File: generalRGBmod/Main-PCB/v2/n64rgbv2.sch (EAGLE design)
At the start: 76 parts, among them J3 2510-, U1 5M570ZT100C5, U2 ADV7125/ADV7123, U4 TLV70018-DDC

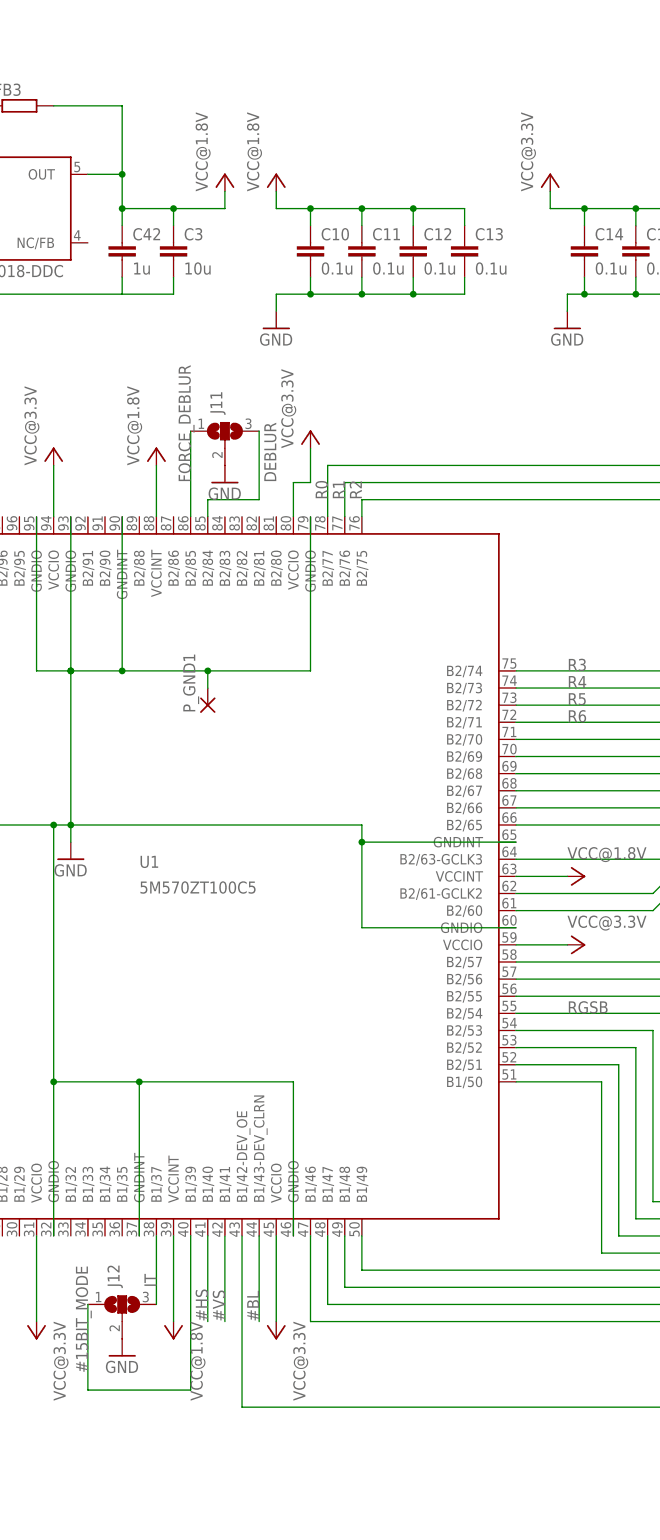
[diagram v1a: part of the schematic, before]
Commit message: N64RGBv1/v2 misc updates  (thanks to iFixRetro for giving feedback here!!!): - bugfix BOM and silkscreen (N64RGBv2) - silkscreen update to distinguish between MaxII and MaxV setup avoiding assembly mistakes - move power regulator to BOT copper side (N64RGBv1) - additional jumper J1 to select between 240LE and 570LE CPLD (for proper usage of the 5M240ZT)
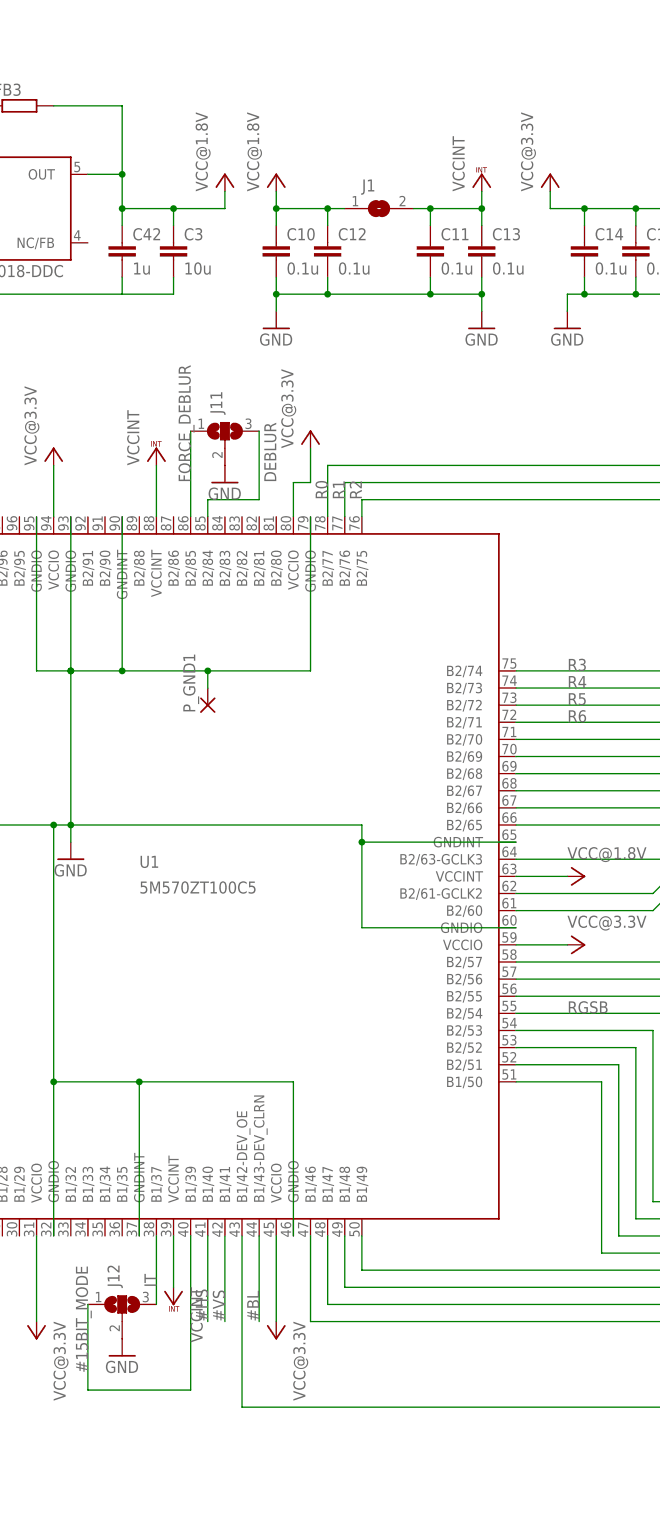
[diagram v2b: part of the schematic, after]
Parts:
- added J1: (no value), jumper:SJ
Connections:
- new net VCCINT: C11.1, C13.1, J1.2, U1.VCCINT@2, U1.VCCINT@3
- net VCC@1.8V: now also J1.1; no longer C11.1, C13.1, U1.VCCINT@2, U1.VCCINT@3
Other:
- moved on the sheet: C10, C11, C12, C13
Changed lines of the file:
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@@
 <?xml version="1.0" encoding="utf-8"?>
 <!DOCTYPE eagle SYSTEM "eagle.dtd">
-<eagle version="8.4.3">
+<eagle version="8.5.0">
 <drawing>
 <settings>
@@
 <part name="C17" library="rcl" deviceset="C-EU" device="C0603" value="0.1u"/>
 <part name="U1" library="altera" deviceset="5M570ZT100C5" device=""/>
-<part name="P+15" library="supply1" library_urn="urn:adsk.eagle:library:371" deviceset="VCC" device="" value="VCC@1.8V"/>
-<part name="P+16" library="supply1" library_urn="urn:adsk.eagle:library:371" deviceset="VCC" device="" value="VCC@1.8V"/>
 <part name="C18" library="rcl" deviceset="C-EU" device="C0603" value="0.1u"/>
 <part name="C19" library="rcl" deviceset="C-EU" device="C0603" value="0.1u"/>
@@
 <part name="J12" library="jumper" deviceset="SJ2W" device=""/>
 <part name="FB3" library="rcl" deviceset="R-EU_" device="R0603"/>
+<part name="VCC1" library="supply1" library_urn="urn:adsk.eagle:library:371" deviceset="VCCINT" device=""/>
+<part name="GND2" library="supply1" library_urn="urn:adsk.eagle:library:371" deviceset="GND" device=""/>
+<part name="VCC2" library="supply1" library_urn="urn:adsk.eagle:library:371" deviceset="VCCINT" device=""/>
+<part name="VCC3" library="supply1" library_urn="urn:adsk.eagle:library:371" deviceset="VCCINT" device=""/>
+<part name="J1" library="jumper" deviceset="SJ" device=""/>
 </parts>
 <sheets>
@@
 <instance part="CTRL" gate="1" x="15.24" y="101.6"/>
 <instance part="RST#" gate="1" x="7.62" y="99.06"/>
-<instance part="C11" gate="G$1" x="175.26" y="215.9"/>
+<instance part="C11" gate="G$1" x="185.42" y="215.9"/>
 <instance part="FB1" gate="G$1" x="78.74" y="220.98"/>
 <instance part="P+3" gate="VCC" x="93.98" y="226.06"/>
@@
 <instance part="P_VCC0" gate="1" x="55.88" y="220.98"/>
 <instance part="P_GND0" gate="1" x="55.88" y="208.28"/>
-<instance part="C12" gate="G$1" x="182.88" y="215.9"/>
-<instance part="C13" gate="G$1" x="190.5" y="215.9"/>
+<instance part="C12" gate="G$1" x="170.18" y="215.9"/>
+<instance part="C13" gate="G$1" x="193.04" y="215.9"/>
 <instance part="C14" gate="G$1" x="208.28" y="215.9"/>
 <instance part="C15" gate="G$1" x="215.9" y="215.9"/>
@@
 <instance part="C17" gate="G$1" x="231.14" y="215.9"/>
 <instance part="U1" gate="G$1" x="144.78" y="121.92"/>
-<instance part="P+15" gate="VCC" x="144.78" y="185.42"/>
-<instance part="P+16" gate="VCC" x="147.32" y="53.34" rot="R180"/>
 <instance part="C18" gate="G$1" x="238.76" y="215.9"/>
 <instance part="C19" gate="G$1" x="246.38" y="215.9"/>
-<instance part="C10" gate="G$1" x="167.64" y="215.9"/>
+<instance part="C10" gate="G$1" x="162.56" y="215.9"/>
 <instance part="C1" gate="G$1" x="66.04" y="215.9"/>
 <instance part="C2" gate="G$1" x="93.98" y="215.9"/>
@@
 <instance part="J12" gate="G$1" x="139.7" y="58.42" rot="R90"/>
 <instance part="FB3" gate="G$1" x="124.46" y="236.22"/>
+<instance part="VCC1" gate="G$1" x="193.04" y="226.06"/>
+<instance part="GND2" gate="1" x="193.04" y="203.2"/>
+<instance part="VCC2" gate="G$1" x="144.78" y="185.42"/>
+<instance part="VCC3" gate="G$1" x="147.32" y="58.42" rot="R180"/>
+<instance part="J1" gate="1" x="177.8" y="220.98"/>
 </instances>
 <busses>
@@
 </segment>
 <segment>
-<pinref part="C11" gate="G$1" pin="2"/>
-<wire x1="175.26" y1="210.82" x2="175.26" y2="208.28" width="0.1524" layer="91"/>
-<wire x1="175.26" y1="208.28" x2="167.64" y2="208.28" width="0.1524" layer="91"/>
-<wire x1="167.64" y1="208.28" x2="162.56" y2="208.28" width="0.1524" layer="91"/>
 <wire x1="162.56" y1="208.28" x2="162.56" y2="205.74" width="0.1524" layer="91"/>
 <pinref part="GND17" gate="1" pin="GND"/>
-<wire x1="167.64" y1="210.82" x2="167.64" y2="208.28" width="0.1524" layer="91"/>
-<junction x="167.64" y="208.28"/>
+<wire x1="162.56" y1="210.82" x2="162.56" y2="208.28" width="0.1524" layer="91"/>
+<junction x="162.56" y="208.28"/>
 <pinref part="C10" gate="G$1" pin="2"/>
+<wire x1="162.56" y1="208.28" x2="170.18" y2="208.28" width="0.1524" layer="91"/>
+<pinref part="C12" gate="G$1" pin="2"/>
+<wire x1="170.18" y1="210.82" x2="170.18" y2="208.28" width="0.1524" layer="91"/>
 <pinref part="C13" gate="G$1" pin="2"/>
-<wire x1="175.26" y1="208.28" x2="182.88" y2="208.28" width="0.1524" layer="91"/>
-<wire x1="182.88" y1="208.28" x2="190.5" y2="208.28" width="0.1524" layer="91"/>
-<wire x1="190.5" y1="208.28" x2="190.5" y2="210.82" width="0.1524" layer="91"/>
-<junction x="175.26" y="208.28"/>
-<pinref part="C12" gate="G$1" pin="2"/>
-<wire x1="182.88" y1="210.82" x2="182.88" y2="208.28" width="0.1524" layer="91"/>
-<junction x="182.88" y="208.28"/>
+<pinref part="GND2" gate="1" pin="GND"/>
+<wire x1="193.04" y1="210.82" x2="193.04" y2="208.28" width="0.1524" layer="91"/>
+<wire x1="193.04" y1="208.28" x2="193.04" y2="205.74" width="0.1524" layer="91"/>
+<wire x1="170.18" y1="208.28" x2="185.42" y2="208.28" width="0.1524" layer="91"/>
+<junction x="170.18" y="208.28"/>
+<junction x="193.04" y="208.28"/>
+<pinref part="C11" gate="G$1" pin="2"/>
+<wire x1="185.42" y1="208.28" x2="193.04" y2="208.28" width="0.1524" layer="91"/>
+<wire x1="185.42" y1="210.82" x2="185.42" y2="208.28" width="0.1524" layer="91"/>
+<junction x="185.42" y="208.28"/>
 </segment>
 <segment>
@@
 <pinref part="P+12" gate="VCC" pin="VCC"/>
 <wire x1="162.56" y1="223.52" x2="162.56" y2="220.98" width="0.1524" layer="91"/>
-<pinref part="C11" gate="G$1" pin="1"/>
-<wire x1="162.56" y1="220.98" x2="167.64" y2="220.98" width="0.1524" layer="91"/>
-<wire x1="167.64" y1="220.98" x2="175.26" y2="220.98" width="0.1524" layer="91"/>
-<wire x1="175.26" y1="220.98" x2="175.26" y2="218.44" width="0.1524" layer="91"/>
-<wire x1="167.64" y1="218.44" x2="167.64" y2="220.98" width="0.1524" layer="91"/>
-<junction x="167.64" y="220.98"/>
+<wire x1="162.56" y1="218.44" x2="162.56" y2="220.98" width="0.1524" layer="91"/>
+<junction x="162.56" y="220.98"/>
 <pinref part="C10" gate="G$1" pin="1"/>
-<pinref part="C13" gate="G$1" pin="1"/>
-<wire x1="175.26" y1="220.98" x2="182.88" y2="220.98" width="0.1524" layer="91"/>
-<wire x1="182.88" y1="220.98" x2="190.5" y2="220.98" width="0.1524" layer="91"/>
-<wire x1="190.5" y1="220.98" x2="190.5" y2="218.44" width="0.1524" layer="91"/>
-<junction x="175.26" y="220.98"/>
+<wire x1="162.56" y1="220.98" x2="170.18" y2="220.98" width="0.1524" layer="91"/>
 <pinref part="C12" gate="G$1" pin="1"/>
-<wire x1="182.88" y1="218.44" x2="182.88" y2="220.98" width="0.1524" layer="91"/>
-<junction x="182.88" y="220.98"/>
-</segment>
-<segment>
-<pinref part="U1" gate="G$1" pin="VCCINT@3"/>
-<pinref part="P+15" gate="VCC" pin="VCC"/>
-<wire x1="144.78" y1="175.26" x2="144.78" y2="182.88" width="0.1524" layer="91"/>
-</segment>
-<segment>
-<pinref part="P+16" gate="VCC" pin="VCC"/>
-<pinref part="U1" gate="G$1" pin="VCCINT@2"/>
-<wire x1="147.32" y1="55.88" x2="147.32" y2="68.58" width="0.1524" layer="91"/>
+<wire x1="170.18" y1="218.44" x2="170.18" y2="220.98" width="0.1524" layer="91"/>
+<wire x1="170.18" y1="220.98" x2="172.72" y2="220.98" width="0.1524" layer="91"/>
+<junction x="170.18" y="220.98"/>
+<pinref part="J1" gate="1" pin="1"/>
 </segment>
 </net>
@@
 </segment>
 </net>
+<net name="VCCINT" class="0">
+<segment>
+<pinref part="VCC1" gate="G$1" pin="VCCINT"/>
+<pinref part="C11" gate="G$1" pin="1"/>
+<pinref part="C13" gate="G$1" pin="1"/>
+<wire x1="193.04" y1="223.52" x2="193.04" y2="220.98" width="0.1524" layer="91"/>
+<pinref part="J1" gate="1" pin="2"/>
+<wire x1="193.04" y1="220.98" x2="193.04" y2="218.44" width="0.1524" layer="91"/>
+<wire x1="182.88" y1="220.98" x2="185.42" y2="220.98" width="0.1524" layer="91"/>
+<junction x="193.04" y="220.98"/>
+<wire x1="185.42" y1="220.98" x2="193.04" y2="220.98" width="0.1524" layer="91"/>
+<wire x1="185.42" y1="218.44" x2="185.42" y2="220.98" width="0.1524" layer="91"/>
+<junction x="185.42" y="220.98"/>
+</segment>
+<segment>
+<pinref part="U1" gate="G$1" pin="VCCINT@3"/>
+<pinref part="VCC2" gate="G$1" pin="VCCINT"/>
+<wire x1="144.78" y1="182.88" x2="144.78" y2="175.26" width="0.1524" layer="91"/>
+</segment>
+<segment>
+<pinref part="U1" gate="G$1" pin="VCCINT@2"/>
+<pinref part="VCC3" gate="G$1" pin="VCCINT"/>
+<wire x1="147.32" y1="60.96" x2="147.32" y2="68.58" width="0.1524" layer="91"/>
+</segment>
+</net>
